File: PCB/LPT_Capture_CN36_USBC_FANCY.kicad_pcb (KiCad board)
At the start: 2 copper layers, 68 x 32 mm, 34 parts, among them J1 GSB1C411101DS1HR, J2 112-036-213R001, Q1 SL2301S, Q2 SL2301S, SW1 SW_DIP_x04, U1 FT245RL

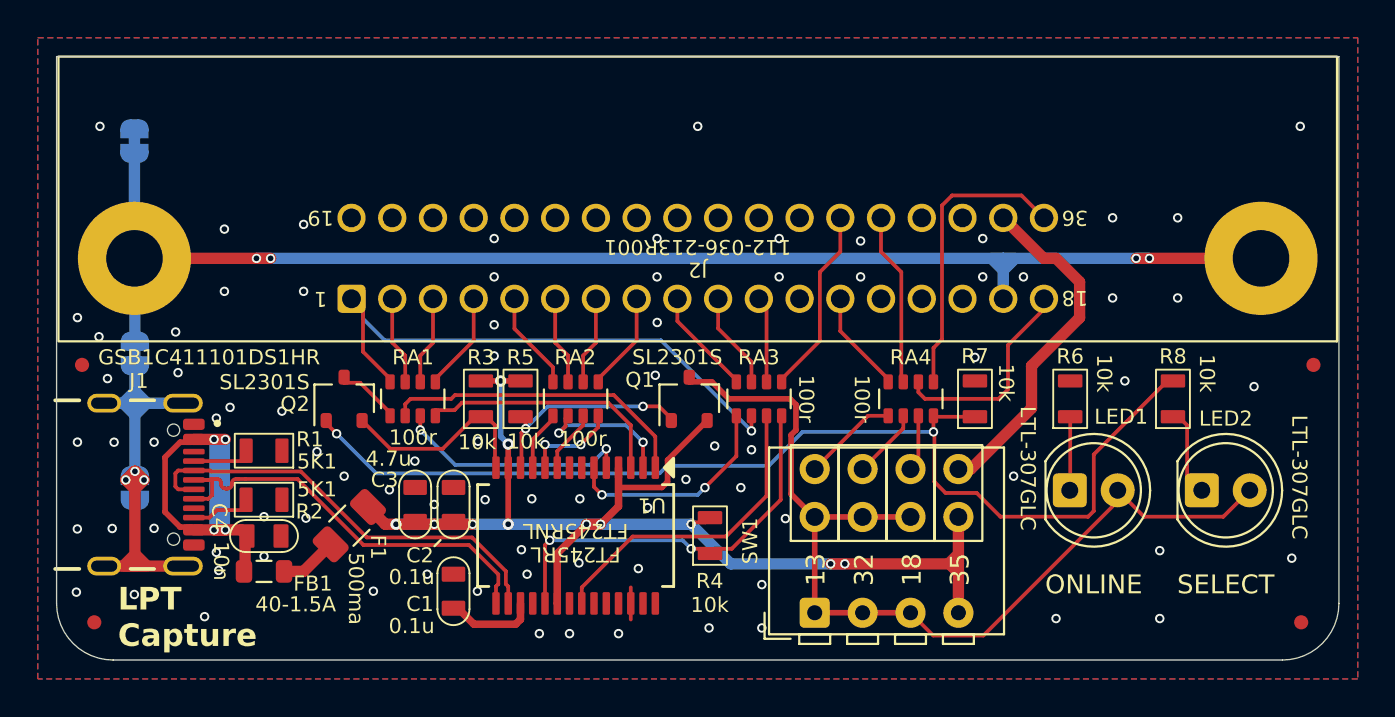
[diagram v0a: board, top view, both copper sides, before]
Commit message: cn36 cover customizer
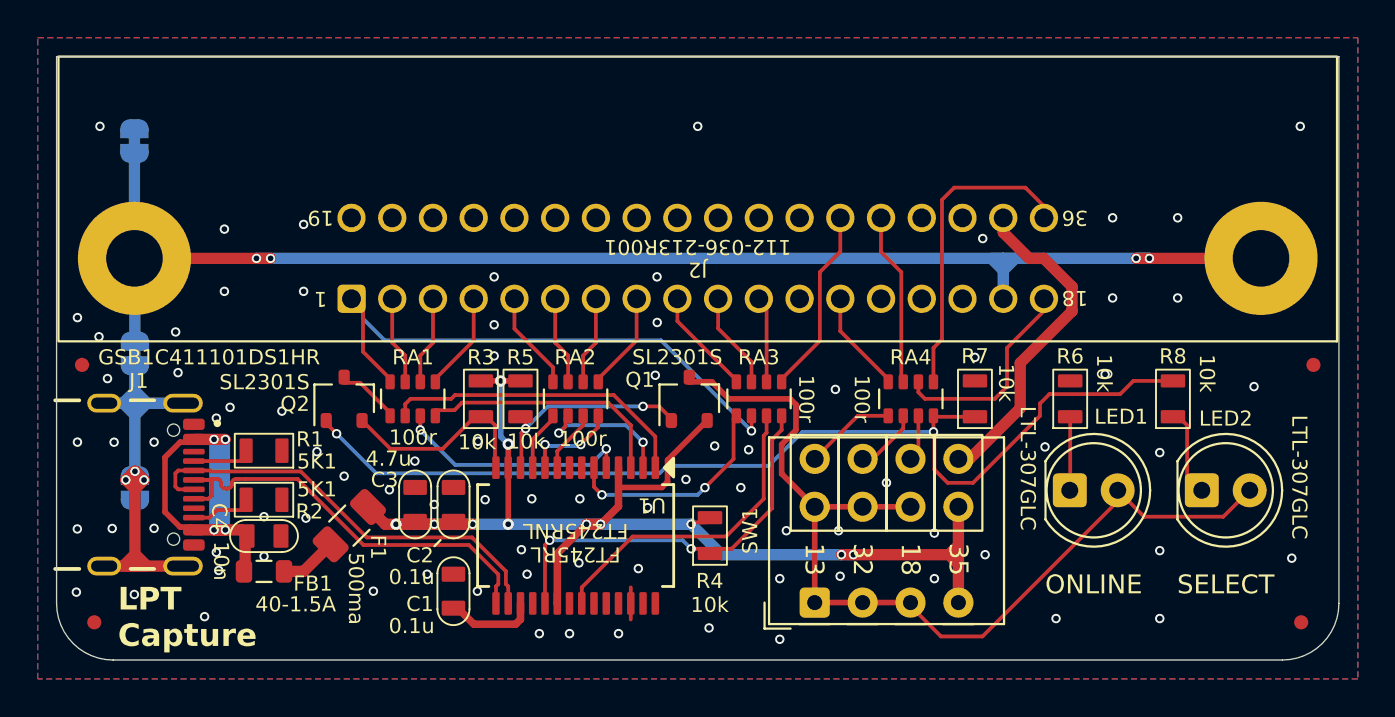
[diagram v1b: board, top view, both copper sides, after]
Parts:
- N1: footprint 000_LOCAL:Housing_CN36_shell_snap -> 000_LOCAL:Housing_CN36
- SW1: footprint 000_LOCAL:SW_DIP_SPSTx04_Piano_Jumper_dual -> 000_LOCAL:SW_DIP_SPST_Jumper_Dual_x04
- moved SW1 0.54 mm to (160.0, 109.1)
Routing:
- net /~{SEL}: track 58.3 -> 55.0 mm
- net /~{SELIN}: track 15.8 -> 16.7 mm
- net /5V: track 18.4 -> 17.6 mm
- net /sPLH: track 3.00 -> 2.46 mm

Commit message: fancy versions - prevent backfeed through online led
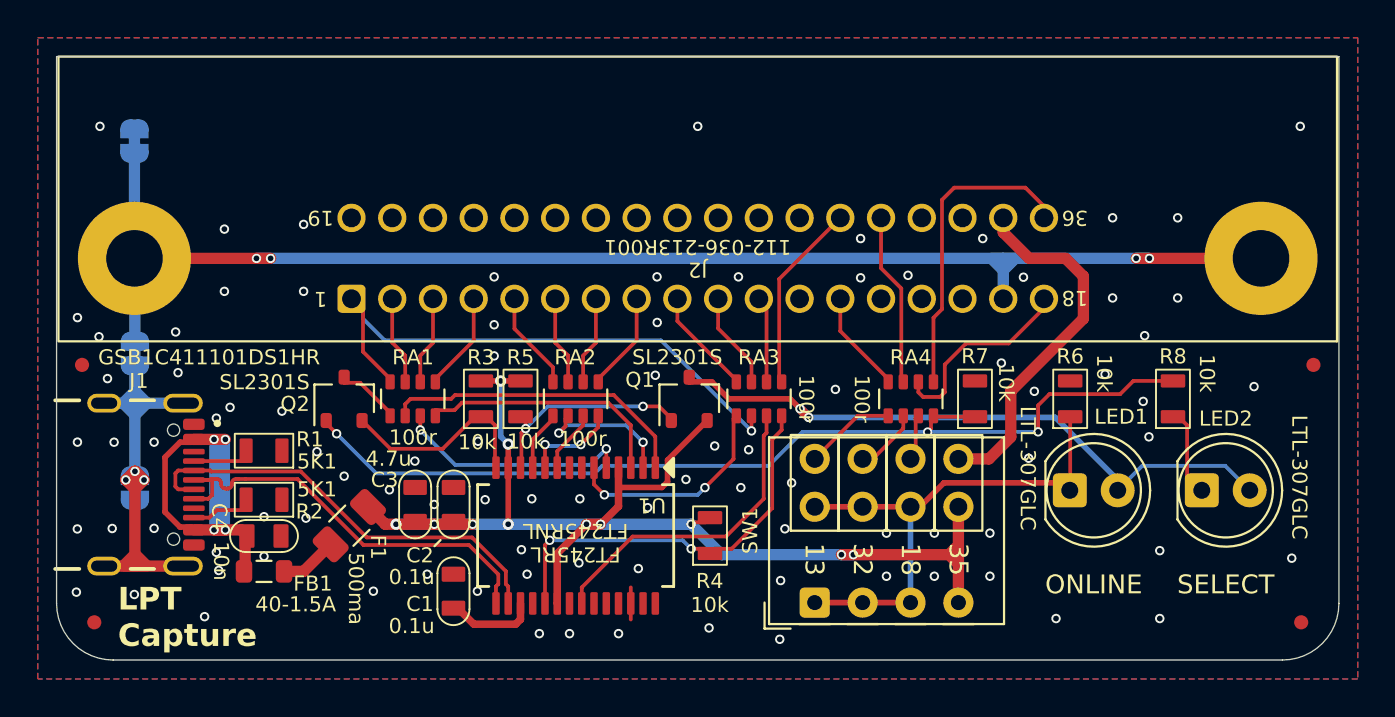
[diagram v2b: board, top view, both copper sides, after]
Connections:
- LED1 pad 1: Net-(LED1-K) -> /ON
- LED1 pad 2: /ON -> Net-(LED1-A)
- LED2 pad 2: /ON -> Net-(LED1-A)
- Q1 pad 3: /ON -> Net-(LED1-A)
- R6 pad 1: Net-(LED1-K) -> /ON
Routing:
- net Net-(LED1-A): track 0.00 -> 35.0 mm, vias 0 -> 2
- net /ON: track 51.6 -> 28.3 mm
- net Net-(LED1-K): track 3.91 -> 0.00 mm
- net /~{SEL}: track 55.0 -> 52.2 mm, vias 2 -> 3
- net /5V: track 17.6 -> 19.4 mm
- net /PLH: track 11.1 -> 10.6 mm
- net GND: vias 84 -> 93

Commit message: cn36 ground paths around sw1
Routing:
- net VCC: track 68.9 -> 70.3 mm
- net /ON: track 28.3 -> 29.1 mm
- net GND: vias 93 -> 90

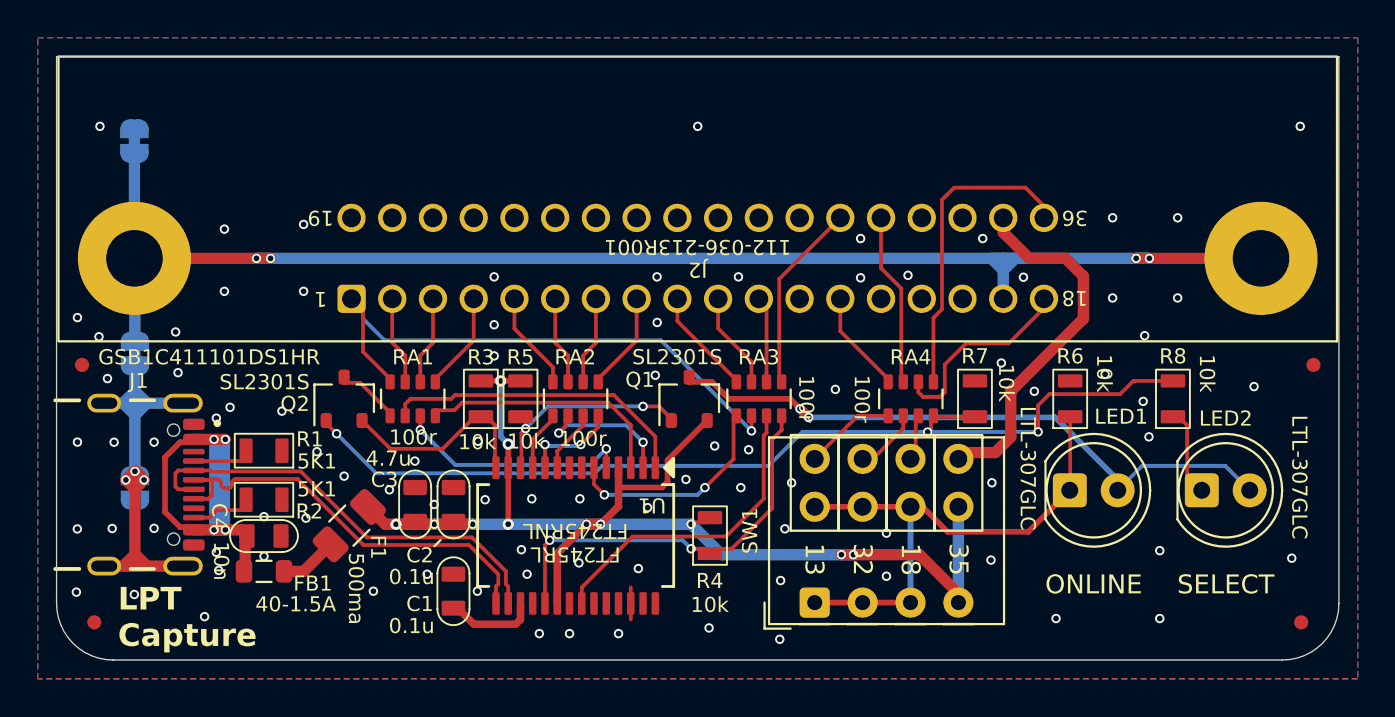
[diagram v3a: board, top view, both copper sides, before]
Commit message: cn36 add reset button
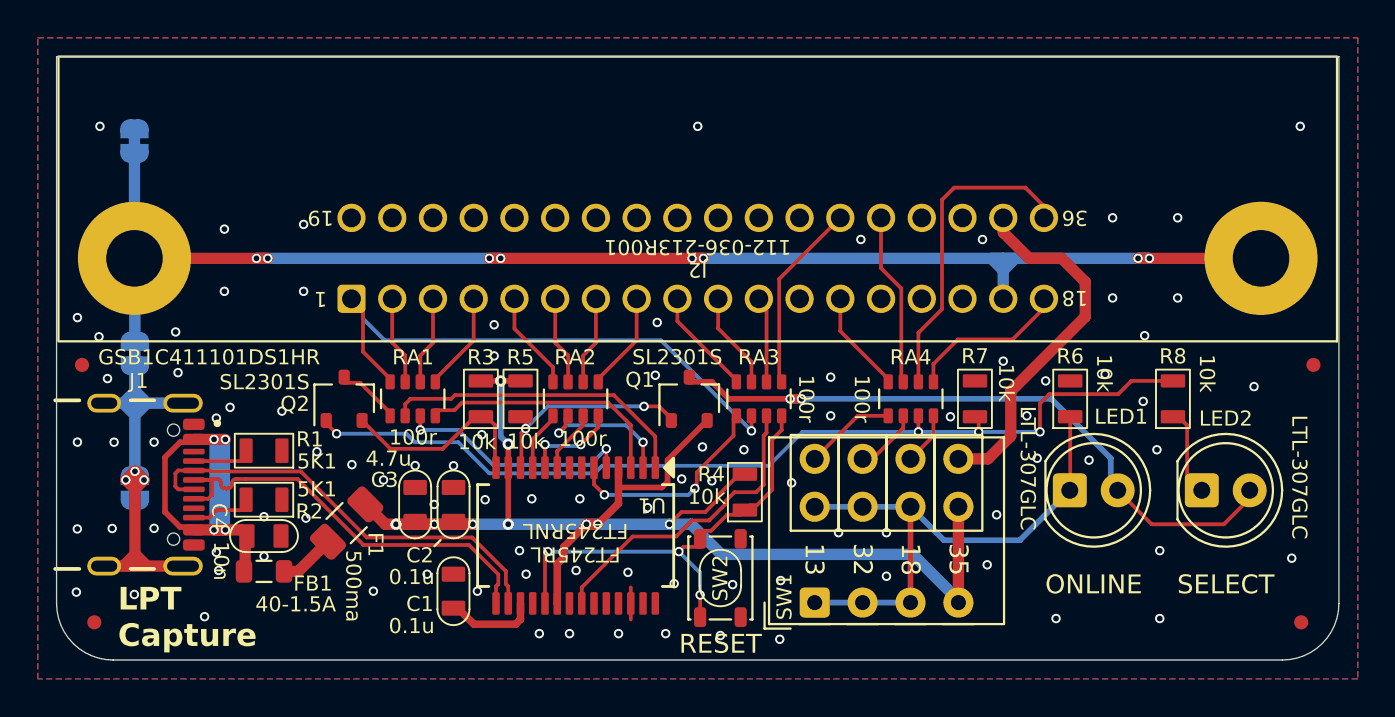
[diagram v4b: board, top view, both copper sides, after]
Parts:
- added SW2: RESET, 000_LOCAL:SW_SPST_PTS810, F.Cu at (151.2, 111.7)
- moved R4 2.95 mm to (152.5, 107.1)
- moved F1 0.20 mm to (131.4, 108.7)
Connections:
- net /sERR renamed /~{sERR}
- net Net-(LED1-A) renamed /PWREN
- RA4 pad 3: /sPLH -> /~{SEL}
- RA4 pad 4: /~{SEL} -> /sPLH
- RA4 pad 5: /~{SELIN} -> /PLH
- RA4 pad 6: /PLH -> /~{SELIN}
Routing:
- net VCC: track 70.3 -> 73.6 mm, vias 11 -> 9
- net /~{RESET}: track 21.6 -> 24.6 mm, vias 2 -> 3
- net /PLH: track 10.6 -> 8.53 mm
- net /~{SEL}: track 52.2 -> 50.8 mm, vias 3 -> 4
- net /PWREN: track 35.0 -> 36.1 mm
- net LPT_SHIELD: track 74.0 -> 74.9 mm, vias 4 -> 8
- net GND: vias 90 -> 93
